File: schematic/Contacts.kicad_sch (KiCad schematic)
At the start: 0 parts

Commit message: Create driver schematic
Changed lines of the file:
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@@
     (effects (font (size 1.27 1.27)) (justify right))
   )
-  (hierarchical_label "A" (shape input) (at 76.2 88.9 180) (fields_autoplaced)
+  (hierarchical_label "A" (shape output) (at 76.2 88.9 180) (fields_autoplaced)
     (effects (font (size 1.27 1.27)) (justify right))
   )
-  (hierarchical_label "B" (shape input) (at 76.2 101.6 180) (fields_autoplaced)
+  (hierarchical_label "B" (shape output) (at 76.2 101.6 180) (fields_autoplaced)
     (effects (font (size 1.27 1.27)) (justify right))
   )

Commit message: Create connector schematic
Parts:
- added J5: ~, Custom:SolderPad-3pin, symbol Custom:SolderPad-3pin
- added J6: ~, Custom:SolderPad-1pin, symbol Custom:SolderPad-1pin
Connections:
- net A: now also J5.1
- net B: now also J5.3
- net Base: now also J6.1
- new net +24V: J5.2
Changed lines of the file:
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@@
 (kicad_sch (version 20230121) (generator eeschema)
   (paper "A4")
-  (hierarchical_label "Base" (shape output) (at 76.2 114.3 180) (fields_autoplaced)
+  (wire (pts (xy 149.86 106.68) (xy 152.4 106.68))
+    (stroke (width 0) (type default))
+  )
+  (wire (pts (xy 149.86 101.6) (xy 152.4 101.6))
+    (stroke (width 0) (type default))
+  )
+  (wire (pts (xy 144.78 104.14) (xy 152.4 104.14))
+    (stroke (width 0) (type default))
+  )
+  (wire (pts (xy 144.78 101.6) (xy 144.78 104.14))
+    (stroke (width 0) (type default))
+  )
+  (wire (pts (xy 149.86 114.3) (xy 152.4 114.3))
+    (stroke (width 0) (type default))
+  )
+  (hierarchical_label "Base" (shape output) (at 149.86 114.3 180) (fields_autoplaced)
     (effects (font (size 1.27 1.27)) (justify right))
   )
-  (hierarchical_label "A" (shape output) (at 76.2 88.9 180) (fields_autoplaced)
+  (hierarchical_label "A" (shape output) (at 149.86 101.6 180) (fields_autoplaced)
     (effects (font (size 1.27 1.27)) (justify right))
   )
-  (hierarchical_label "B" (shape output) (at 76.2 101.6 180) (fields_autoplaced)
+  (hierarchical_label "B" (shape output) (at 149.86 106.68 180) (fields_autoplaced)
     (effects (font (size 1.27 1.27)) (justify right))
   )
+  (symbol (lib_id "Custom:SolderPad-3pin") (at 152.4 104.14 0) (mirror y) (unit 1)
+    (in_bom no) (on_board yes) (dnp no) (fields_autoplaced)
+    (property "Reference" "J5" (at 157.48 104.775 0)
+      (effects (font (size 1.27 1.27)) (justify right))
+    )
+    (property "Value" "~" (at 152.4 101.6 0)
+      (effects (font (size 1.27 1.27)))
+    )
+    (property "Footprint" "Custom:SolderPad-3pin" (at 152.4 109.22 0)
+      (effects (font (size 1.27 1.27)) hide)
+    )
+    (property "Datasheet" "" (at 152.4 101.6 0)
+      (effects (font (size 1.27 1.27)) hide)
+    )
+    (pin "1")
+    (pin "2")
+    (pin "3")
+    (instances
+      (project "uTesla"
+        (path "/0cecab2b-a552-4f9c-b012-66fc2b7d8bdb/13104c3d-b875-4e02-970f-7d210569d6e3"
+          (reference "J5") (unit 1)
+        )
+      )
+    )
+  )
+  (symbol (lib_id "power:+24V") (at 144.78 101.6 0) (unit 1)
+    (in_bom yes) (on_board yes) (dnp no) (fields_autoplaced)
+    (property "Reference" "#PWR046" (at 144.78 105.41 0)
+      (effects (font (size 1.27 1.27)) hide)
+    )
+    (property "Value" "+24V" (at 144.78 97.79 0)
+      (effects (font (size 1.27 1.27)))
+    )
+    (property "Footprint" "" (at 144.78 101.6 0)
+      (effects (font (size 1.27 1.27)) hide)
+    )
+    (property "Datasheet" "" (at 144.78 101.6 0)
+      (effects (font (size 1.27 1.27)) hide)
+    )
+    (pin "1")
+    (instances
+      (project "uTesla"
+        (path "/0cecab2b-a552-4f9c-b012-66fc2b7d8bdb/13104c3d-b875-4e02-970f-7d210569d6e3"
+          (reference "#PWR046") (unit 1)
+        )
+      )
+    )
+  )
+  (symbol (lib_id "Custom:SolderPad-1pin") (at 152.4 114.3 0) (mirror y) (unit 1)
+    (in_bom no) (on_board yes) (dnp no) (fields_autoplaced)
+    (property "Reference" "J6" (at 157.48 114.935 0)
+      (effects (font (size 1.27 1.27)) (justify right))
+    )
+    (property "Value" "~" (at 152.4 114.3 0)
+      (effects (font (size 1.27 1.27)))
+    )
+    (property "Footprint" "Custom:SolderPad-1pin" (at 152.4 116.84 0)
+      (effects (font (size 1.27 1.27)) hide)
+    )
+    (property "Datasheet" "" (at 152.4 114.3 0)
+      (effects (font (size 1.27 1.27)) hide)
+    )
+    (pin "1")
+    (instances
+      (project "uTesla"
+        (path "/0cecab2b-a552-4f9c-b012-66fc2b7d8bdb/13104c3d-b875-4e02-970f-7d210569d6e3"
+          (reference "J6") (unit 1)
+        )
+      )
+    )
+  )
 )

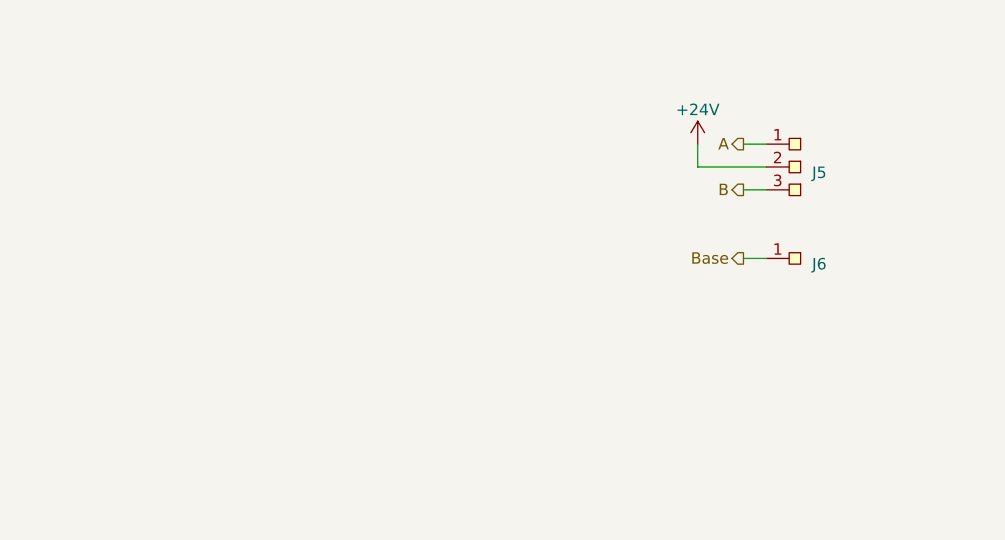
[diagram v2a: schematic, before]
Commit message: Add grounding solder pads
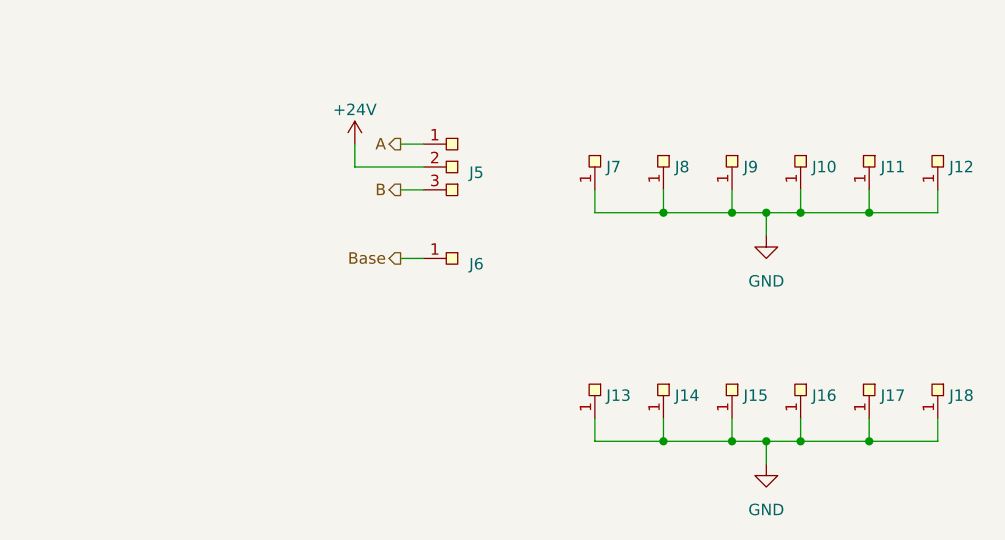
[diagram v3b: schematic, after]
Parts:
- added J10, J11, J12, J13, J14, J15, J16, J17, J18, J7, J8, J9: ~, Custom:SolderPad-1pin, symbol Custom:SolderPad-1pin
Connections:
- new net GND: J10.1, J11.1, J12.1, J13.1, J14.1, J15.1, J16.1, J17.1, J18.1, J7.1, J8.1, J9.1
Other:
- moved on the sheet: J5, J6
